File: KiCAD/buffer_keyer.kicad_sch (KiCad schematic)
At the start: 90 parts, among them J1 Conn_01x02_Pin, J13 Conn_01x05, J16 Conn_01x05, T1 2N3906, T2 2N3906, U15 LM7805_TO220, U19 L79L08_TO92, U20 ICL7660S, U3 MC1496, U4 MCP4921, U6 LM7171xIN, U7 LM7171xIN, U8 MCP4728

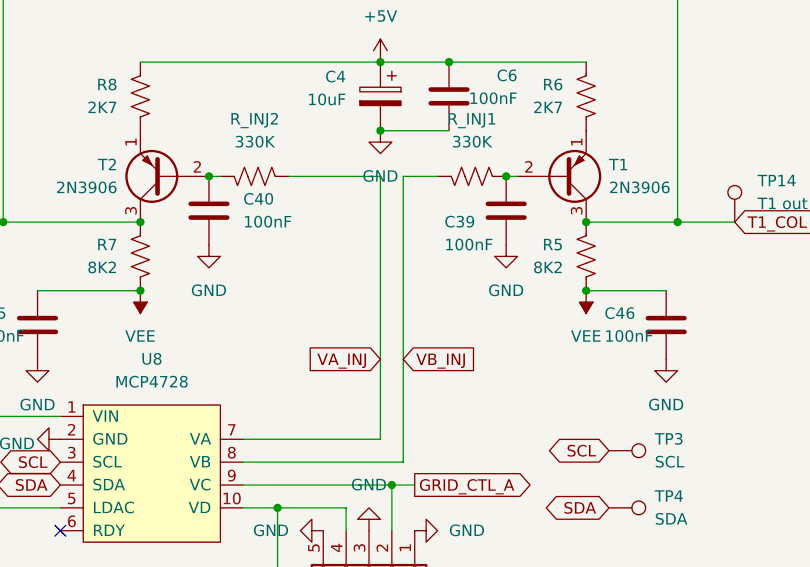
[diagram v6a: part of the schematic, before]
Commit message: kicad: routing progress + VA/VB filter caps + LM7805 bulk cap
- Add 100nF filter caps at R_INJ inputs (VA/VB) to block long-trace
  RF pickup at MC1496 carrier-null network
- Add 10uF bulk cap at LM7805 output (C35 too far to serve this role)
- More traces routed on buffer_keyer, some VA/VB routing on B.Cu to
  clear L2/L4 toroid area

Co-Authored-By: Claude Opus 4.7 <noreply@anthropic.com>
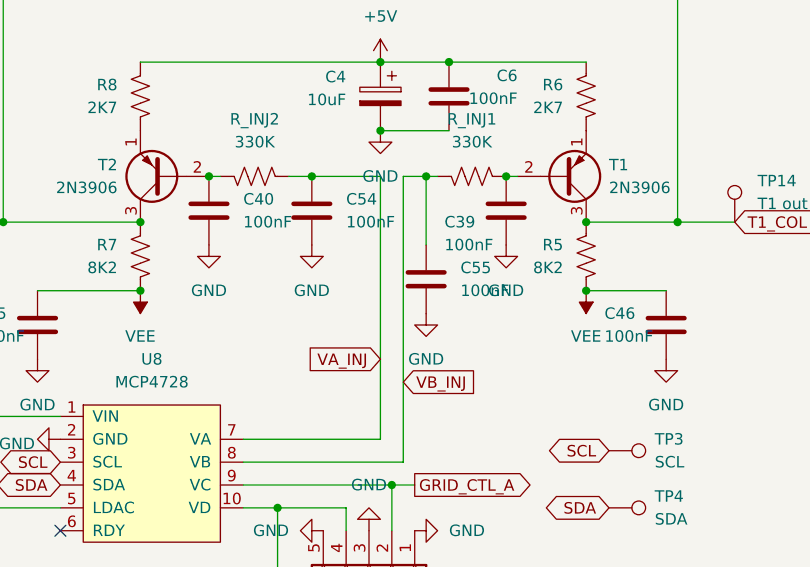
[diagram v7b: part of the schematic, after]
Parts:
- added C54, C55: 100nF, Capacitor_THT:C_Disc_D5.0mm_W2.5mm_P5.00mm, symbol Device:C
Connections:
- net GND: now also C54.2, C55.2
- net VA_INJ: now also C54.1
- net VB_INJ: now also C55.1

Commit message: kicad: fix L7 to Device:L symbol, add JFET gate leak on VFO
- buffer_keyer.kicad_sch: L7 (22uH choke) now uses Device:L symbol
  instead of Device:R. Netlist and footprint unchanged; symbol now
  renders as inductor loops instead of resistor rectangle.
- vfo.kicad_sch + PCB: added 10K gate-leak resistor at Q1 (J310 buffer)
  to provide DC gate reference. Was missing from KiCad implementation
  but present in QUCS reference schematic as RGL 1M (10K is fine).
- 5 initial mounting holes placed on PCB (positions will be reworked in
  the next commit).

Co-Authored-By: Claude Opus 4.7 <noreply@anthropic.com>
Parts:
- L7: symbol Device:R -> Device:L
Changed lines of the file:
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@@
 	)
 	(symbol
-		(lib_id "Device:R")
+		(lib_id "Device:L")
 		(at 190.5 128.27 90)
 		(unit 1)
